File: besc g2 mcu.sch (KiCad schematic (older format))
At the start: 37 parts

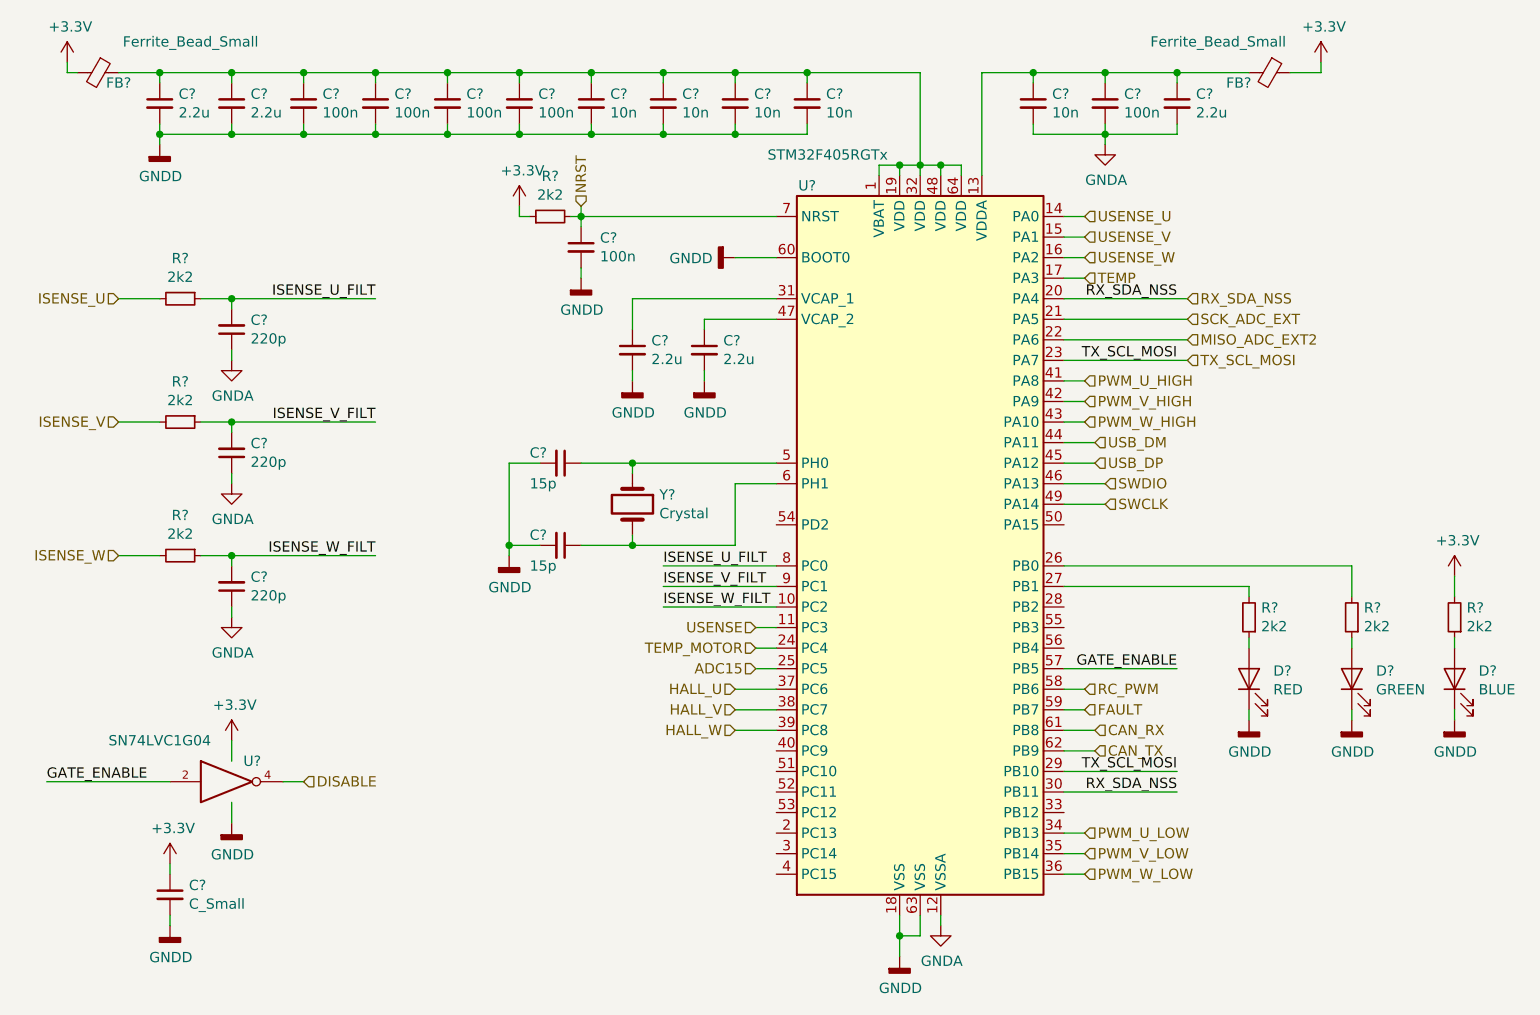
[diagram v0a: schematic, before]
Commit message: power stage layout draft
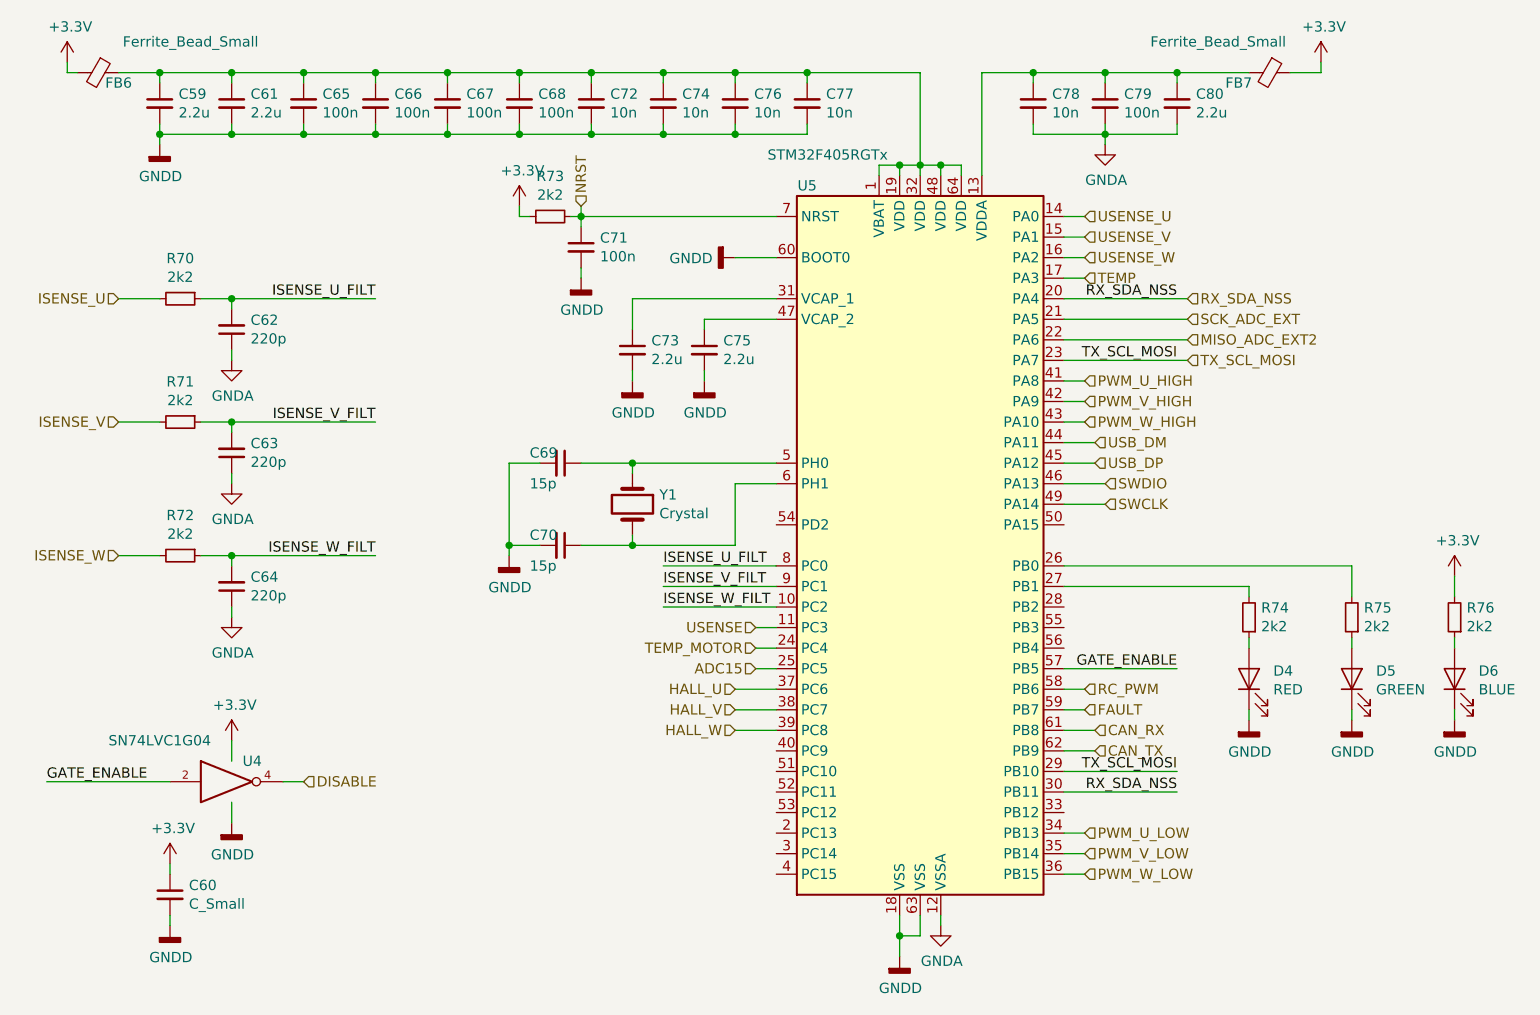
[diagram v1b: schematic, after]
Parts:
- C59, C60, C61, C62, C63, C64, C65, C66, C67, C68, C69, C70, C71, C72, C73, C74, C75, C76, C77, C78, C79, C80: renamed from C?; footprint (none) -> Capacitor_SMD:C_0603_1608Metric
- D4, D5, D6: renamed from D?; footprint (none) -> LED_SMD:LED_0603_1608Metric
- FB6, FB7: renamed from FB?; footprint (none) -> Inductor_SMD:L_0603_1608Metric
- R70, R71, R72, R73, R74, R75, R76: renamed from R?; footprint (none) -> Resistor_SMD:R_0603_1608Metric
- U4: renamed from U?; footprint (none) -> Package_TO_SOT_SMD:SOT-23-5
- Y1: renamed from Y?; footprint (none) -> Crystal:Crystal_SMD_3225-4Pin_3.2x2.5mm
- gave numbers to parts that had none: 1

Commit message: isolated drivers, layout
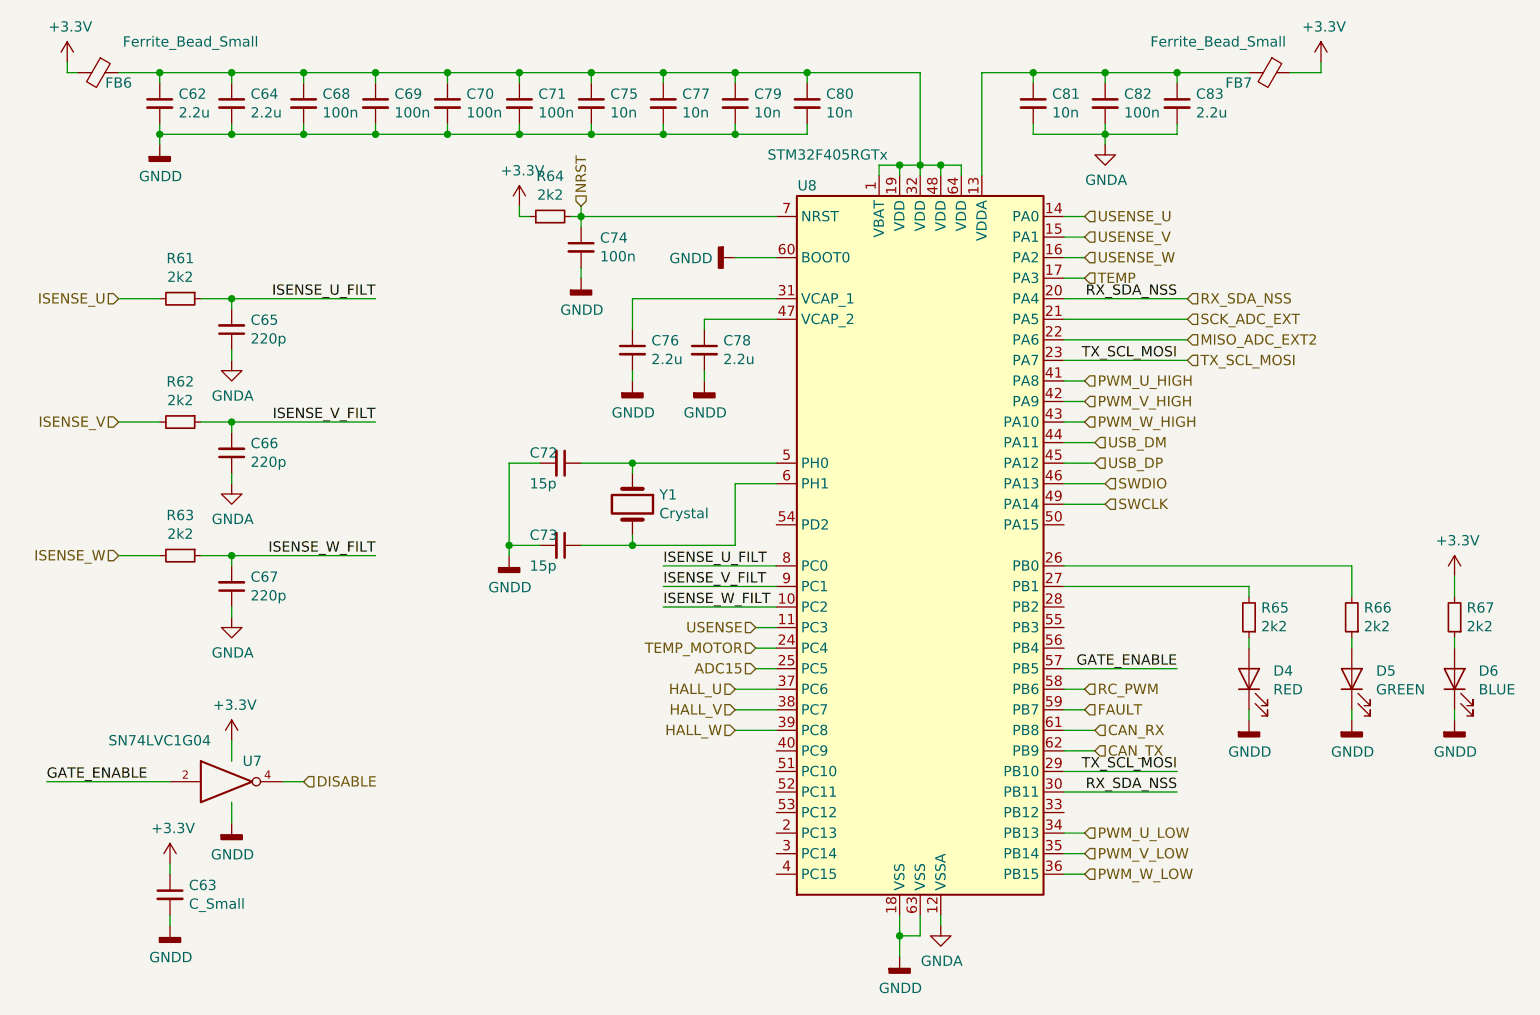
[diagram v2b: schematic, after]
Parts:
- renumbered C59 to C62, C60 to C63, C61 to C64, C62 to C65, C63 to C66, C64 to C67, C65 to C68, C66 to C69, C67 to C70, C68 to C71, C69 to C72, C70 to C73, C71 to C74, C72 to C75, C73 to C76, C74 to C77, C75 to C78, C76 to C79, C77 to C80, C78 to C81, C79 to C82, C80 to C83, R70 to R61, R71 to R62, R72 to R63, R73 to R64, R74 to R65, R75 to R66, R76 to R67, U4 to U7, U5 to U8

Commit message: 12V PS, isolated gate drivers
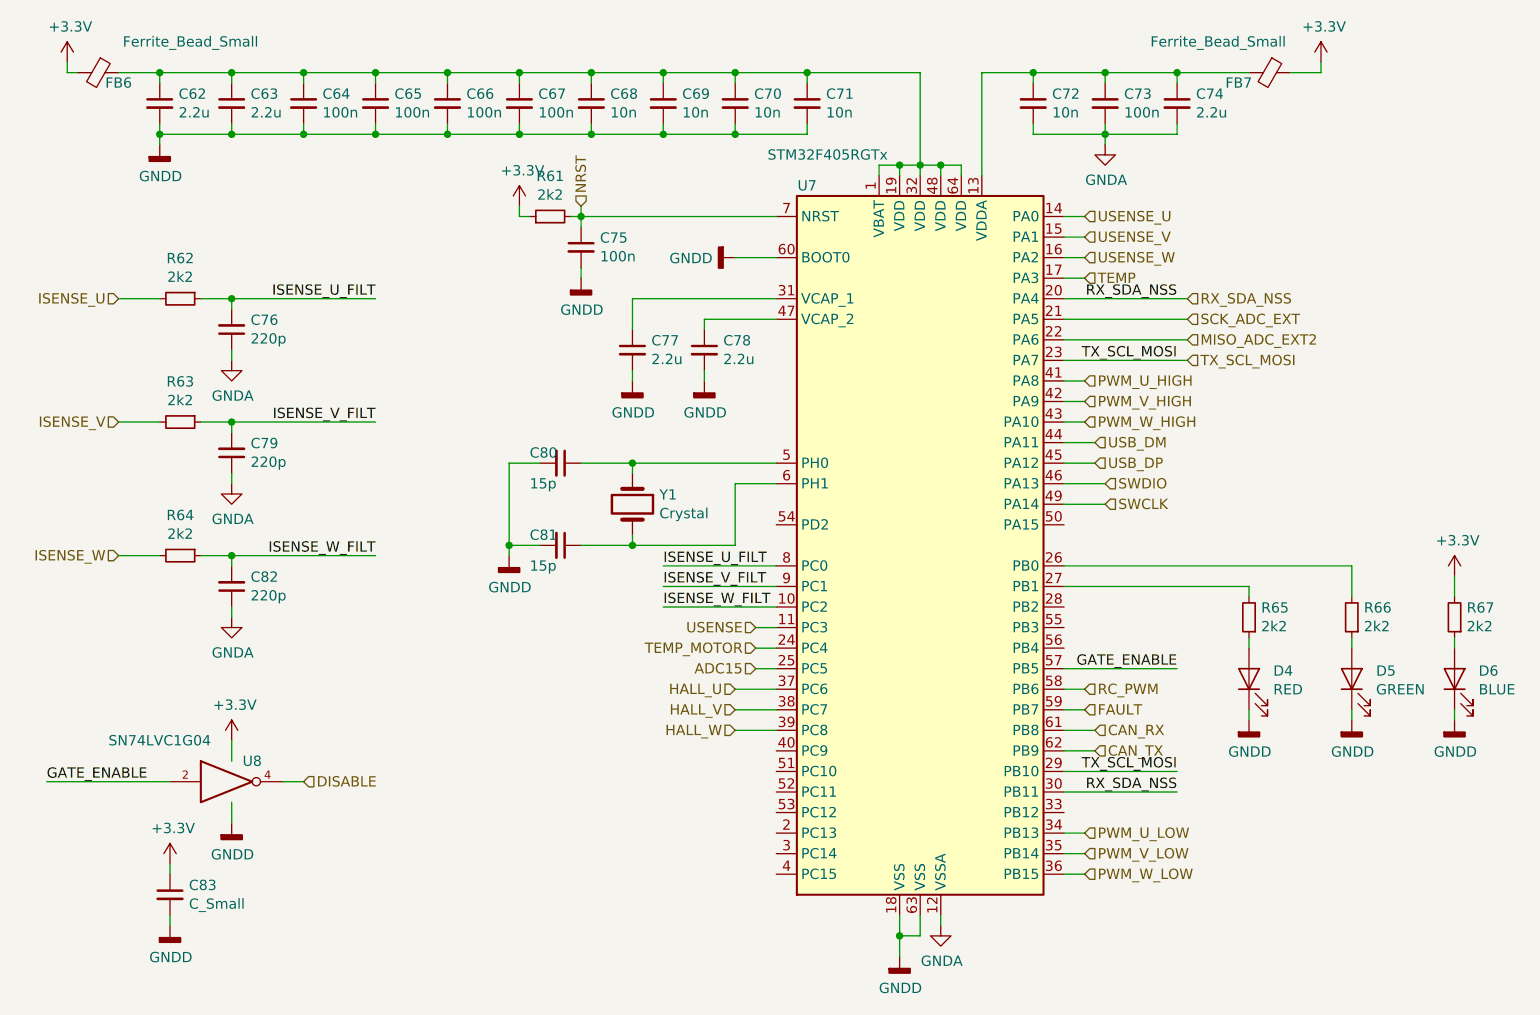
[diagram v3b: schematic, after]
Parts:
- renumbered C64 to C63, C68 to C64, C69 to C65, C70 to C66, C71 to C67, C75 to C68, C77 to C69, C79 to C70, C80 to C71, C81 to C72, C82 to C73, C83 to C74, C74 to C75, C65 to C76, C76 to C77, C66 to C79, C72 to C80, C73 to C81, C67 to C82, C63 to C83, R64 to R61, R61 to R62, R62 to R63, R63 to R64, U8 to U7, U7 to U8
